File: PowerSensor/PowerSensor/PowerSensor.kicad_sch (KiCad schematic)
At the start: 12 parts, among them J1 Screw_Terminal_01x02, J3 BAT+, J4 BAT-, J5 Screw_Terminal_01x04, U1 ACS712ELCTR-20A-T_NRND

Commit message: PCB last optimization
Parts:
- J1: value Screw_Terminal_01x02 -> Current Sens
- J5: footprint (none) -> TerminalBlock:TerminalBlock_bornier-4_P5.08mm
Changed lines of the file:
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@@
       (effects (font (size 1.27 1.27)))
     )
-    (property "Value" "Screw_Terminal_01x02" (at 158.75 102.87 0)
+    (property "Value" "Current Sens" (at 158.75 102.87 0)
       (effects (font (size 1.27 1.27)))
     )
@@
       (effects (font (size 1.27 1.27)))
     )
-    (property "Footprint" "" (at 158.75 147.32 0)
-      (effects (font (size 1.27 1.27)) hide)
-    )
+    (property "Footprint" "TerminalBlock:TerminalBlock_bornier-4_P5.08mm" (at 158.75 147.32 0)
+      (effects (font (size 1.27 1.27)) hide)
+    )

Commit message: Change the filter Cap value 1nF
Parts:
- C2: value C -> 1nF
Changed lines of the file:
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@@
       (effects (font (size 1.27 1.27)) (justify left))
     )
-    (property "Value" "C" (at 237.49 68.58 0)
+    (property "Value" "1nF" (at 237.49 68.58 0)
       (effects (font (size 1.27 1.27)) (justify left))
     )

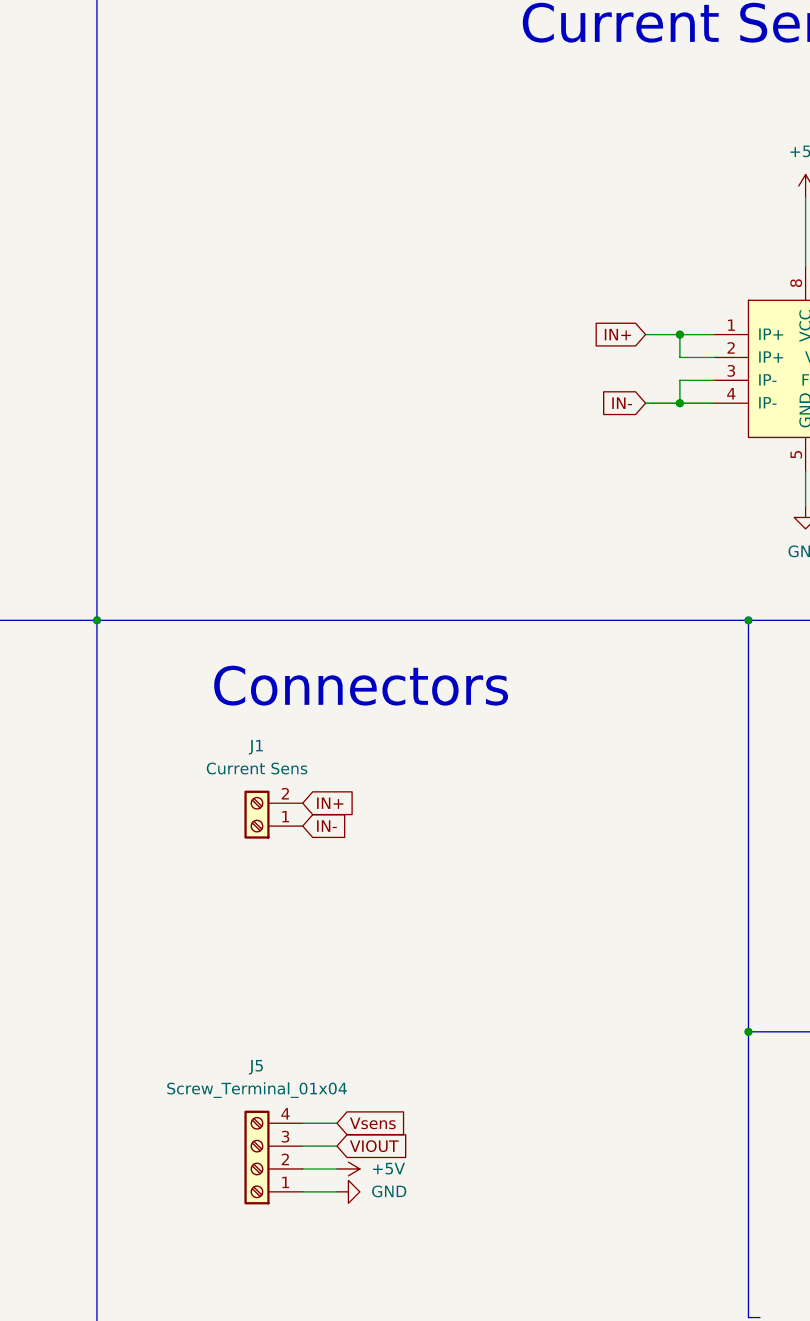
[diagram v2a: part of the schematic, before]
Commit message: Add voltage divider to current sensor output ( to Reduce Inrush Current)
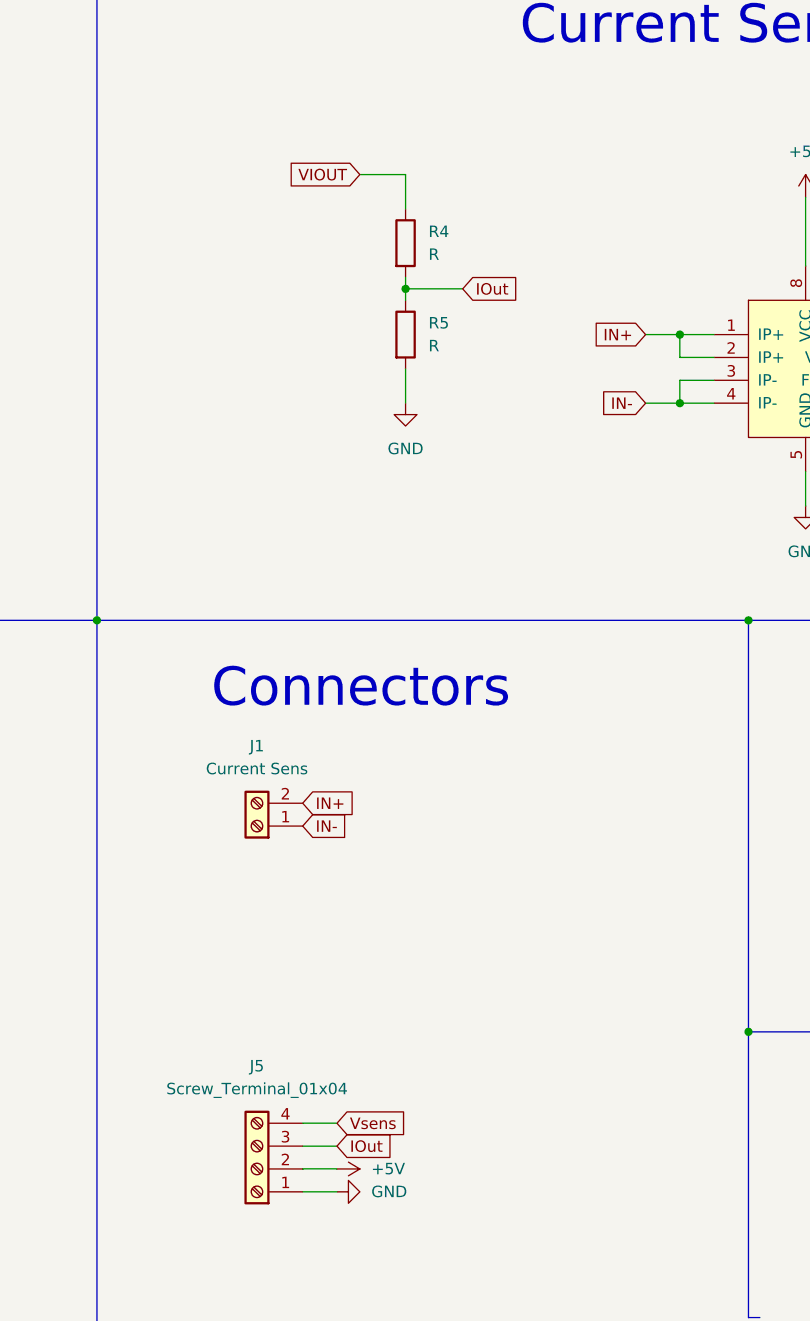
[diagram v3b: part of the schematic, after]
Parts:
- added R4, R5: R, symbol Device:R
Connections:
- net GND: now also R5.2
- net VIOUT: now also R4.1; no longer J5.3 (Pin_3)
- new net IOut: J5.3 (Pin_3), R4.2, R5.1
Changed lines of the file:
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@@
   (junction (at 53.34 125.73) (diameter 0) (color 0 0 0 0)
   )
+  (junction (at 175.26 49.53) (diameter 0) (color 0 0 0 0)
+  )
   (junction (at 228.6 110.49) (diameter 0) (color 0 0 0 0)
   )
@@
     (stroke (width 0) (type default))
   )
+  (wire (pts (xy 175.26 49.53) (xy 181.61 49.53))
+    (stroke (width 0) (type default))
+  )
   (wire (pts (xy 228.6 110.49) (xy 228.6 113.03))
     (stroke (width 0) (type default))
   )
+  (wire (pts (xy 175.26 36.83) (xy 170.18 36.83))
+    (stroke (width 0) (type default))
+  )
   (wire (pts (xy 219.71 69.85) (xy 219.71 73.66))
     (stroke (width 0) (type default))
@@
     (stroke (width 0) (type default))
   )
+  (wire (pts (xy 175.26 40.64) (xy 175.26 36.83))
+    (stroke (width 0) (type default))
+  )
+  (wire (pts (xy 175.26 58.42) (xy 175.26 62.23))
+    (stroke (width 0) (type default))
+  )
   (wire (pts (xy 233.68 59.69) (xy 233.68 63.5))
     (stroke (width 0) (type default))
@@
     (stroke (width 0) (type default))
   )
+  (wire (pts (xy 175.26 49.53) (xy 175.26 50.8))
+    (stroke (width 0) (type default))
+  )
   (wire (pts (xy 80.01 55.88) (xy 80.01 57.15))
     (stroke (width 0) (type default))
@@
   )
   (wire (pts (xy 205.74 57.15) (xy 205.74 54.61))
+    (stroke (width 0) (type default))
+  )
+  (wire (pts (xy 175.26 48.26) (xy 175.26 49.53))
     (stroke (width 0) (type default))
   )
@@
     )
   )
+  (global_label "IOut" (shape input) (at 181.61 49.53 0) (fields_autoplaced)
+    (effects (font (size 1.27 1.27)) (justify left))
+    (property "Intersheetrefs" "${INTERSHEET_REFS}" (at 188.4052 49.53 0)
+      (effects (font (size 1.27 1.27)) (justify left) hide)
+    )
+  )
   (global_label "Vsens" (shape input) (at 90.17 57.15 0) (fields_autoplaced)
     (effects (font (size 1.27 1.27)) (justify left))
     (property "Intersheetrefs" "${INTERSHEET_REFS}" (at 98.5376 57.15 0)
       (effects (font (size 1.27 1.27)) (justify left) hide)
+    )
+  )
+  (global_label "VIOUT" (shape input) (at 170.18 36.83 180) (fields_autoplaced)
+    (effects (font (size 1.27 1.27)) (justify right))
+    (property "Intersheetrefs" "${INTERSHEET_REFS}" (at 161.8728 36.83 0)
+      (effects (font (size 1.27 1.27)) (justify right) hide)
     )
   )
@@
     )
   )
+  (global_label "IOut" (shape input) (at 167.64 144.78 0) (fields_autoplaced)
+    (effects (font (size 1.27 1.27)) (justify left))
+    (property "Intersheetrefs" "${INTERSHEET_REFS}" (at 174.4352 144.78 0)
+      (effects (font (size 1.27 1.27)) (justify left) hide)
+    )
+  )
   (global_label "IN-" (shape input) (at 201.93 62.23 180) (fields_autoplaced)
     (effects (font (size 1.27 1.27)) (justify right))
@@
     )
   )
-  (global_label "VIOUT" (shape input) (at 167.64 144.78 0) (fields_autoplaced)
-    (effects (font (size 1.27 1.27)) (justify left))
-    (property "Intersheetrefs" "${INTERSHEET_REFS}" (at 175.9472 144.78 0)
-      (effects (font (size 1.27 1.27)) (justify left) hide)
-    )
-  )
   (symbol (lib_id "Device:R") (at 246.38 152.4 90) (unit 1)
     (in_bom yes) (on_board yes) (dnp no) (fields_autoplaced)
@@
     )
   )
+  (symbol (lib_id "Device:R") (at 175.26 54.61 0) (unit 1)
+    (in_bom yes) (on_board yes) (dnp no) (fields_autoplaced)
+    (property "Reference" "R5" (at 177.8 53.34 0)
+      (effects (font (size 1.27 1.27)) (justify left))
+    )
+    (property "Value" "R" (at 177.8 55.88 0)
+      (effects (font (size 1.27 1.27)) (justify left))
+    )
+    (property "Footprint" "" (at 173.482 54.61 90)
+      (effects (font (size 1.27 1.27)) hide)
+    )
+    (property "Datasheet" "~" (at 175.26 54.61 0)
+      (effects (font (size 1.27 1.27)) hide)
+    )
+    (pin "1")
+    (pin "2")
+    (instances
+      (project "PowerSensor"
+        (path "/273ab69c-9da7-4ae5-8226-b4245c0688ed"
+          (reference "R5") (unit 1)
+        )
+      )
+    )
+  )
   (symbol (lib_id "Connector:Screw_Terminal_01x02") (at 44.45 128.27 180) (unit 1)
     (in_bom yes) (on_board yes) (dnp no) (fields_autoplaced)
@@
         (path "/273ab69c-9da7-4ae5-8226-b4245c0688ed"
           (reference "R2") (unit 1)
+        )
+      )
+    )
+  )
+  (symbol (lib_id "Device:R") (at 175.26 44.45 0) (unit 1)
+    (in_bom yes) (on_board yes) (dnp no) (fields_autoplaced)
+    (property "Reference" "R4" (at 177.8 43.18 0)
+      (effects (font (size 1.27 1.27)) (justify left))
+    )
+    (property "Value" "R" (at 177.8 45.72 0)
+      (effects (font (size 1.27 1.27)) (justify left))
+    )
+    (property "Footprint" "" (at 173.482 44.45 90)
+      (effects (font (size 1.27 1.27)) hide)
+    )
+    (property "Datasheet" "~" (at 175.26 44.45 0)
+      (effects (font (size 1.27 1.27)) hide)
+    )
+    (pin "1")
+    (pin "2")
+    (instances
+      (project "PowerSensor"
+        (path "/273ab69c-9da7-4ae5-8226-b4245c0688ed"
+          (reference "R4") (unit 1)
         )
       )
@@
         )
       )
+    )
+  )
+  (symbol (lib_id "power:GND") (at 175.26 62.23 0) (unit 1)
+    (in_bom yes) (on_board yes) (dnp no) (fields_autoplaced)
+    (property "Reference" "#PWR08" (at 175.26 68.58 0)
+      (effects (font (size 1.27 1.27)) hide)
+    )
+    (property "Value" "GND" (at 175.26 67.31 0)
+      (effects (font (size 1.27 1.27)))
+    )
+    (property "Footprint" "" (at 175.26 62.23 0)
+      (effects (font (size 1.27 1.27)) hide)
+    )
+    (property "Datasheet" "" (at 175.26 62.23 0)
+      (effects (font (size 1.27 1.27)) hide)
+    )
+    (pin "1")
+    (instances
+      (project "PowerSensor"
+        (path "/273ab69c-9da7-4ae5-8226-b4245c0688ed"
+          (reference "#PWR08") (unit 1)
+        )
+      )

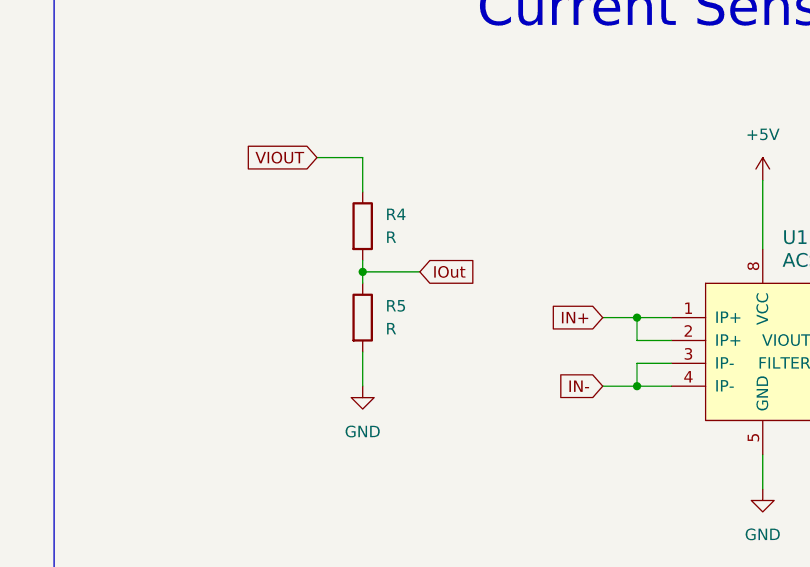
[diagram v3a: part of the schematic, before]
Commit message: Change the voltage divider values
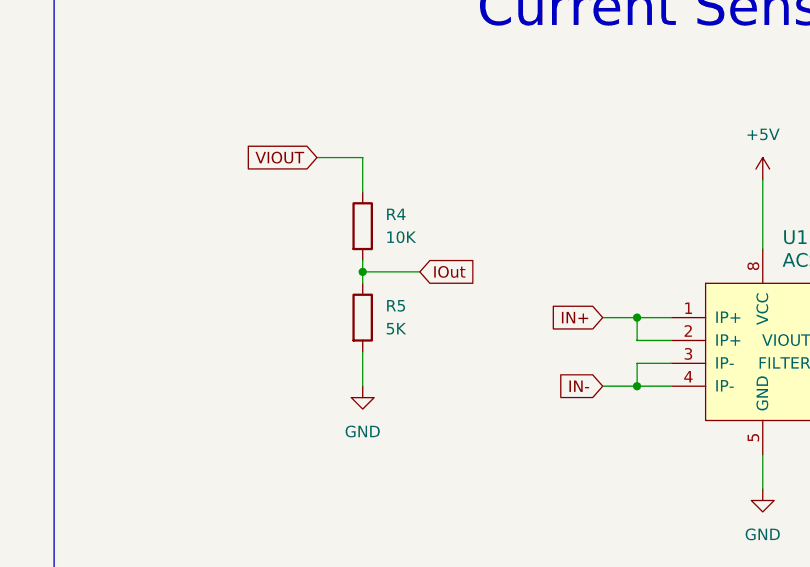
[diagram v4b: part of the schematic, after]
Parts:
- R4: value R -> 10K; footprint (none) -> Resistor_SMD:R_0805_2012Metric
- R5: value R -> 5K; footprint (none) -> Resistor_SMD:R_0805_2012Metric
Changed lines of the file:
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@@
       (effects (font (size 1.27 1.27)) (justify left))
     )
-    (property "Value" "R" (at 177.8 55.88 0)
+    (property "Value" "5K" (at 177.8 55.88 0)
       (effects (font (size 1.27 1.27)) (justify left))
     )
-    (property "Footprint" "" (at 173.482 54.61 90)
+    (property "Footprint" "Resistor_SMD:R_0805_2012Metric" (at 173.482 54.61 90)
       (effects (font (size 1.27 1.27)) hide)
     )
@@
       (effects (font (size 1.27 1.27)) (justify left))
     )
-    (property "Value" "R" (at 177.8 45.72 0)
+    (property "Value" "10K" (at 177.8 45.72 0)
       (effects (font (size 1.27 1.27)) (justify left))
     )
-    (property "Footprint" "" (at 173.482 44.45 90)
+    (property "Footprint" "Resistor_SMD:R_0805_2012Metric" (at 173.482 44.45 90)
       (effects (font (size 1.27 1.27)) hide)
     )
